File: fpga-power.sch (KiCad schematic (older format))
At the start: 71 parts, among them U1 XC7K70T-FBG484

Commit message: Update MPNs, add BOM
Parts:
- U1: MPN (none) -> XC7K70T-1FBG484C; Manufacturer (none) -> Xilinx
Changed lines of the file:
@@
 F 2 "lpddr4-test-board-footprints:BGA484C100P22X22_2300X2300X244N" H 10550 5375 50  0001 C CNN
 F 3 "" H 10550 5375 50  0000 C CNN
+F 4 "XC7K70T-1FBG484C" H 10550 5375 50  0001 C CNN "MPN"
+F 5 "Xilinx" H 10550 5375 50  0001 C CNN "Manufacturer"
 	7    10550 5375
 	1    0    0    -1
@@
 F 2 "lpddr4-test-board-footprints:BGA484C100P22X22_2300X2300X244N" H 13975 4725 50  0001 C CNN
 F 3 "" H 13975 4725 50  0000 C CNN
+F 4 "XC7K70T-1FBG484C" H 13975 4725 50  0001 C CNN "MPN"
+F 5 "Xilinx" H 13975 4725 50  0001 C CNN "Manufacturer"
 	5    13975 4725
 	1    0    0    -1
@@
 F 2 "lpddr4-test-board-footprints:BGA484C100P22X22_2300X2300X244N" H 14000 6750 50  0001 C CNN
 F 3 "" H 14000 6750 50  0000 C CNN
+F 4 "XC7K70T-1FBG484C" H 14000 6750 50  0001 C CNN "MPN"
+F 5 "Xilinx" H 14000 6750 50  0001 C CNN "Manufacturer"
 	4    14000 6750
 	1    0    0    -1

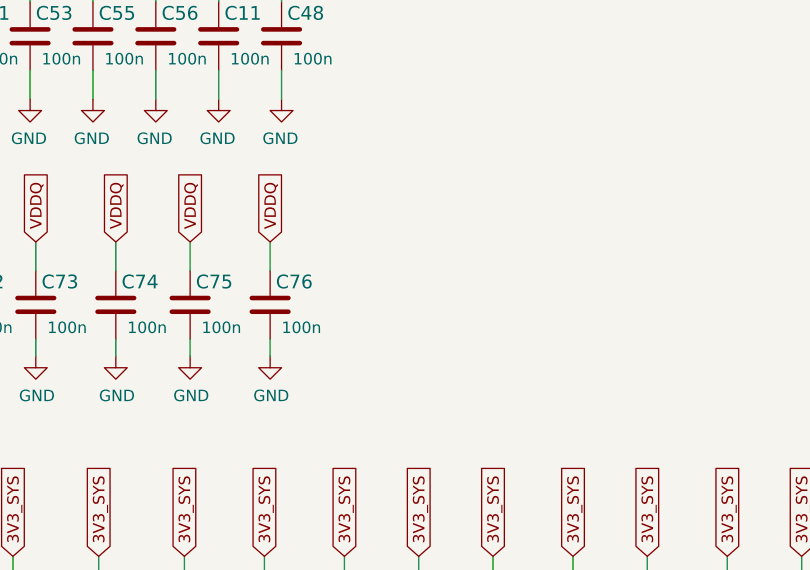
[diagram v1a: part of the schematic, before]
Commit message: Spread LPDDR4 signals on In2.Cu layer
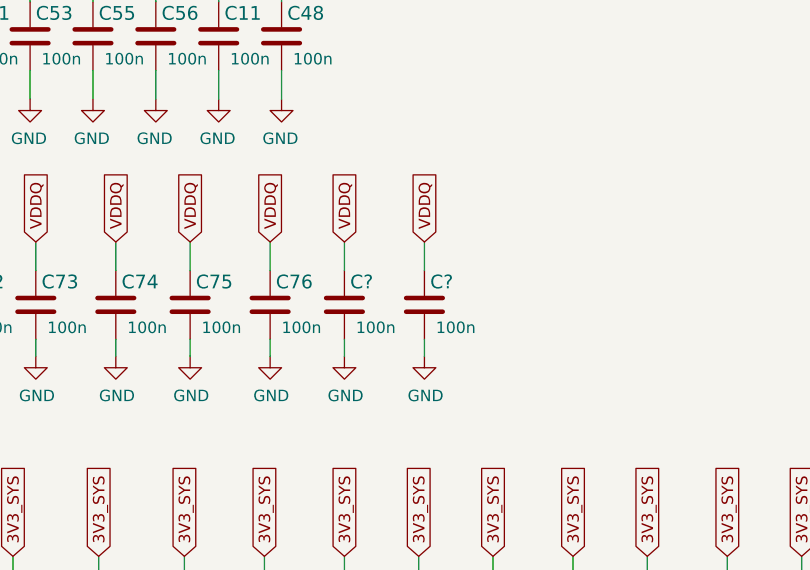
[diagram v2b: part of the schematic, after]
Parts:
- added C? (x2): C_100n_0201, lpddr4-test-board-footprints:0201-res, symbol lpddr4-test-board:C_100n_0201
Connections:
- net GND: now also C?.2, C?.2
- net VDDQ: now also C?.1, C?.1
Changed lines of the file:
@@
 	1    0    0    -1
 $EndComp
+$Comp
+L lpddr4-test-board:C_100n_0201 C?
+U 1 1 60DDB800
+P 4625 7700
+F 0 "C?" H 4650 7800 60  0000 L CNN
+F 1 "C_100n_0201" H 4625 7550 60  0001 C CNN
+F 2 "lpddr4-test-board-footprints:0201-res" H 4825 7900 60  0001 L CNN
+F 3 "" H 4625 7700 50  0001 C CNN
+F 4 "YAGEO" H 4825 8100 60  0001 L CNN "Manufacturer"
+F 5 "CC0201KRX6S5BB104" H 4825 8000 60  0001 L CNN "MPN"
+F 6 "100n" H 4675 7600 50  0000 L CNN "Val"
+	1    4625 7700
+	1    0    0    -1
+$EndComp
+$Comp
+L lpddr4-test-board:GND #PWR?
+U 1 1 60DDB806
+P 4625 7925
+AR Path="/5F96C515/60DDB806" Ref="#PWR?"  Part="1"
+AR Path="/600295C1/60DDB806" Ref="#PWR?"  Part="1"
+F 0 "#PWR?" H 4625 7675 50  0001 C CNN
+F 1 "GND" H 4630 7752 50  0000 C CNN
+F 2 "" H 4625 7925 50  0001 C CNN
+F 3 "" H 4625 7925 50  0001 C CNN
+	1    4625 7925
+	1    0    0    -1
+$EndComp
+Text GLabel 4625 7425 1    50   Input ~ 0
+VDDQ
+Wire Wire Line
+	4625 7425 4625 7550
+Wire Wire Line
+	4625 7850 4625 7925
+$Comp
+L lpddr4-test-board:C_100n_0201 C?
+U 1 1 60DDB812
+P 4975 7700
+F 0 "C?" H 5000 7800 60  0000 L CNN
+F 1 "C_100n_0201" H 4975 7550 60  0001 C CNN
+F 2 "lpddr4-test-board-footprints:0201-res" H 5175 7900 60  0001 L CNN
+F 3 "" H 4975 7700 50  0001 C CNN
+F 4 "YAGEO" H 5175 8100 60  0001 L CNN "Manufacturer"
+F 5 "CC0201KRX6S5BB104" H 5175 8000 60  0001 L CNN "MPN"
+F 6 "100n" H 5025 7600 50  0000 L CNN "Val"
+	1    4975 7700
+	1    0    0    -1
+$EndComp
+$Comp
+L lpddr4-test-board:GND #PWR?
+U 1 1 60DDB818
+P 4975 7925
+AR Path="/5F96C515/60DDB818" Ref="#PWR?"  Part="1"
+AR Path="/600295C1/60DDB818" Ref="#PWR?"  Part="1"
+F 0 "#PWR?" H 4975 7675 50  0001 C CNN
+F 1 "GND" H 4980 7752 50  0000 C CNN
+F 2 "" H 4975 7925 50  0001 C CNN
+F 3 "" H 4975 7925 50  0001 C CNN
+	1    4975 7925
+	1    0    0    -1
+$EndComp
+Text GLabel 4975 7425 1    50   Input ~ 0
+VDDQ
+Wire Wire Line
+	4975 7425 4975 7550
+Wire Wire Line
+	4975 7850 4975 7925
 $EndSCHEMATC
